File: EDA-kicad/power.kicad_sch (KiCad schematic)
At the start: 109 parts, among them Q10 NMOS, Q3 NMOS, Q3_BAT1 NMOS, Q4 NMOS, Q4_BAT1 NMOS, Q5 NMOS, Q6 NMOS, Q7 NMOS, Q8 NMOS, Q9 NMOS, SW6 CHP-041B, U10 BAT-CONNECTOR-FLTS22WR00, U11 BQ25792RQMR, U2 TPS650250RHBR

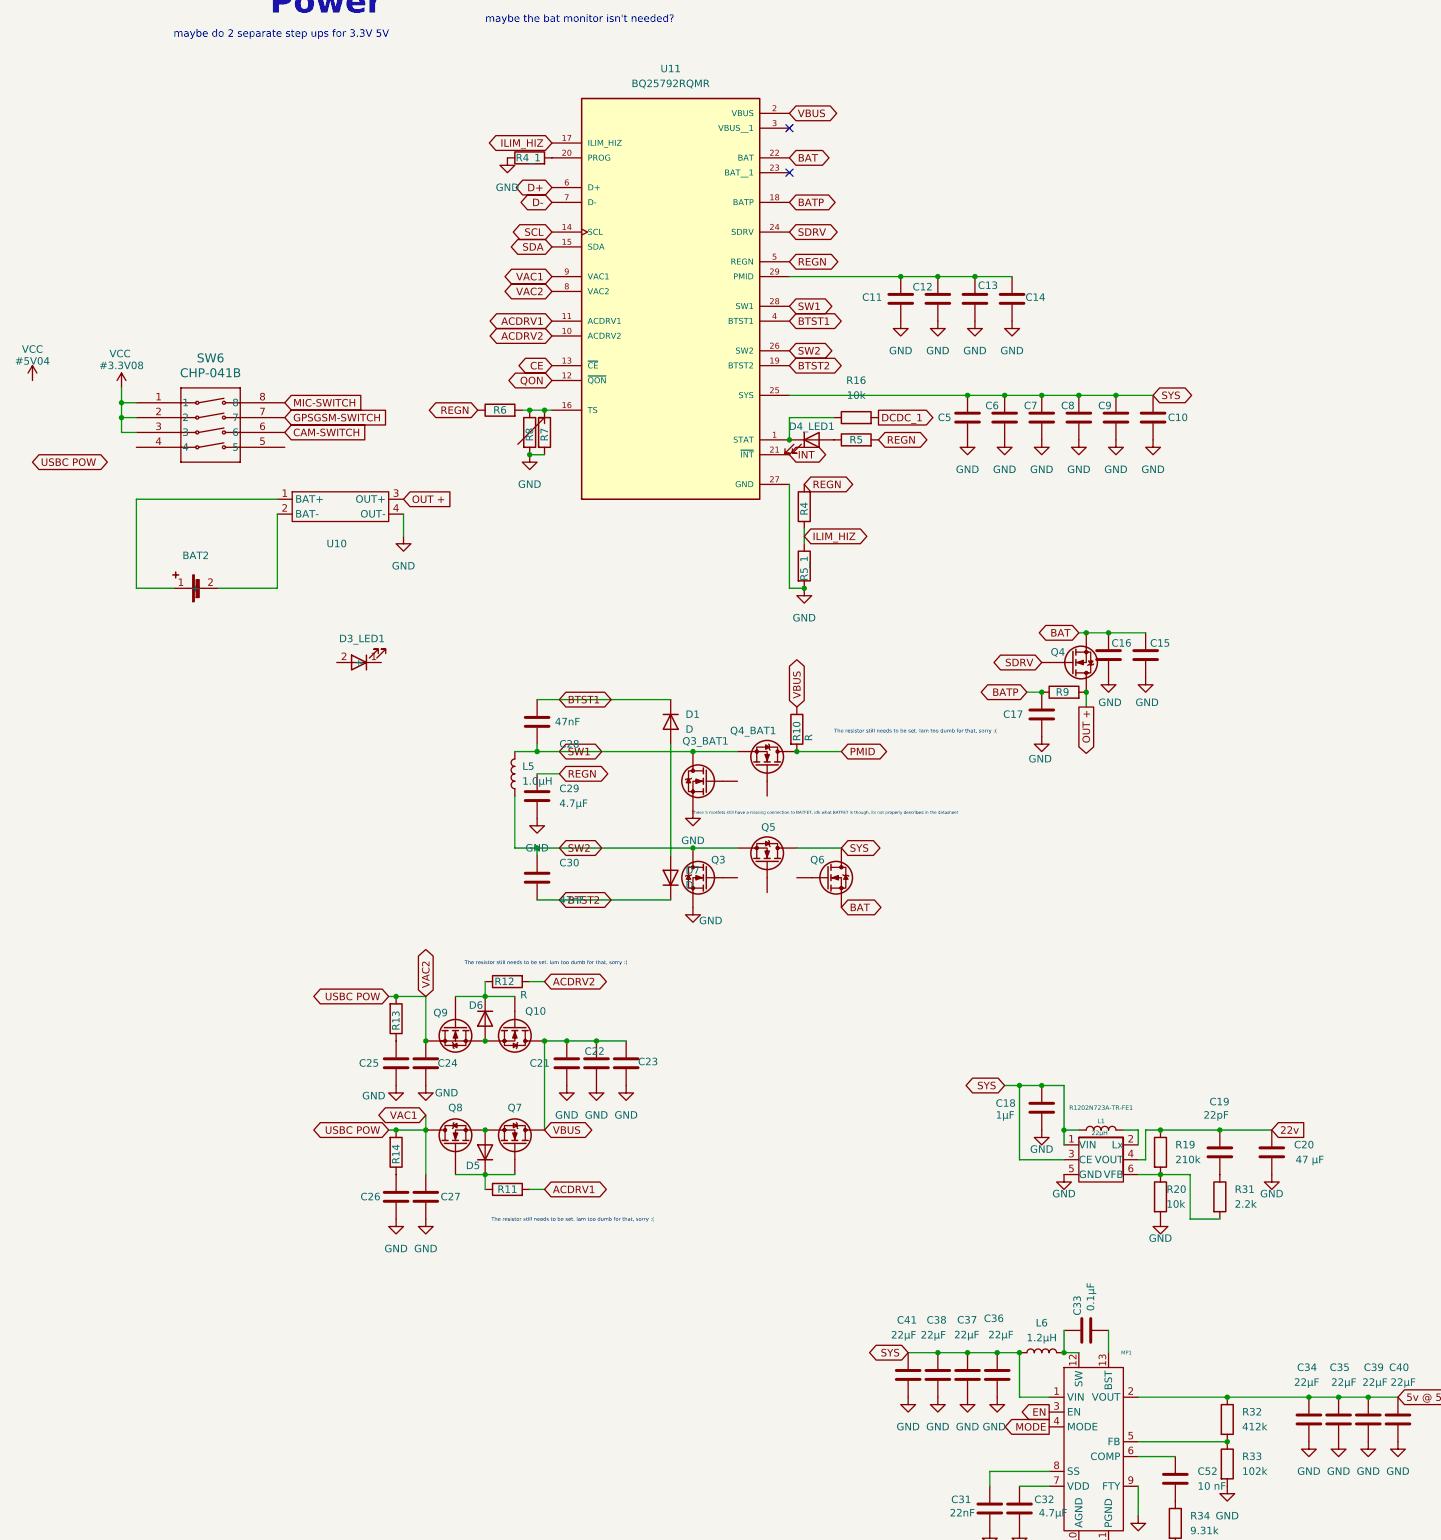
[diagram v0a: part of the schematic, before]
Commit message: fix STAT pin LED, connect USB POW, remove d3
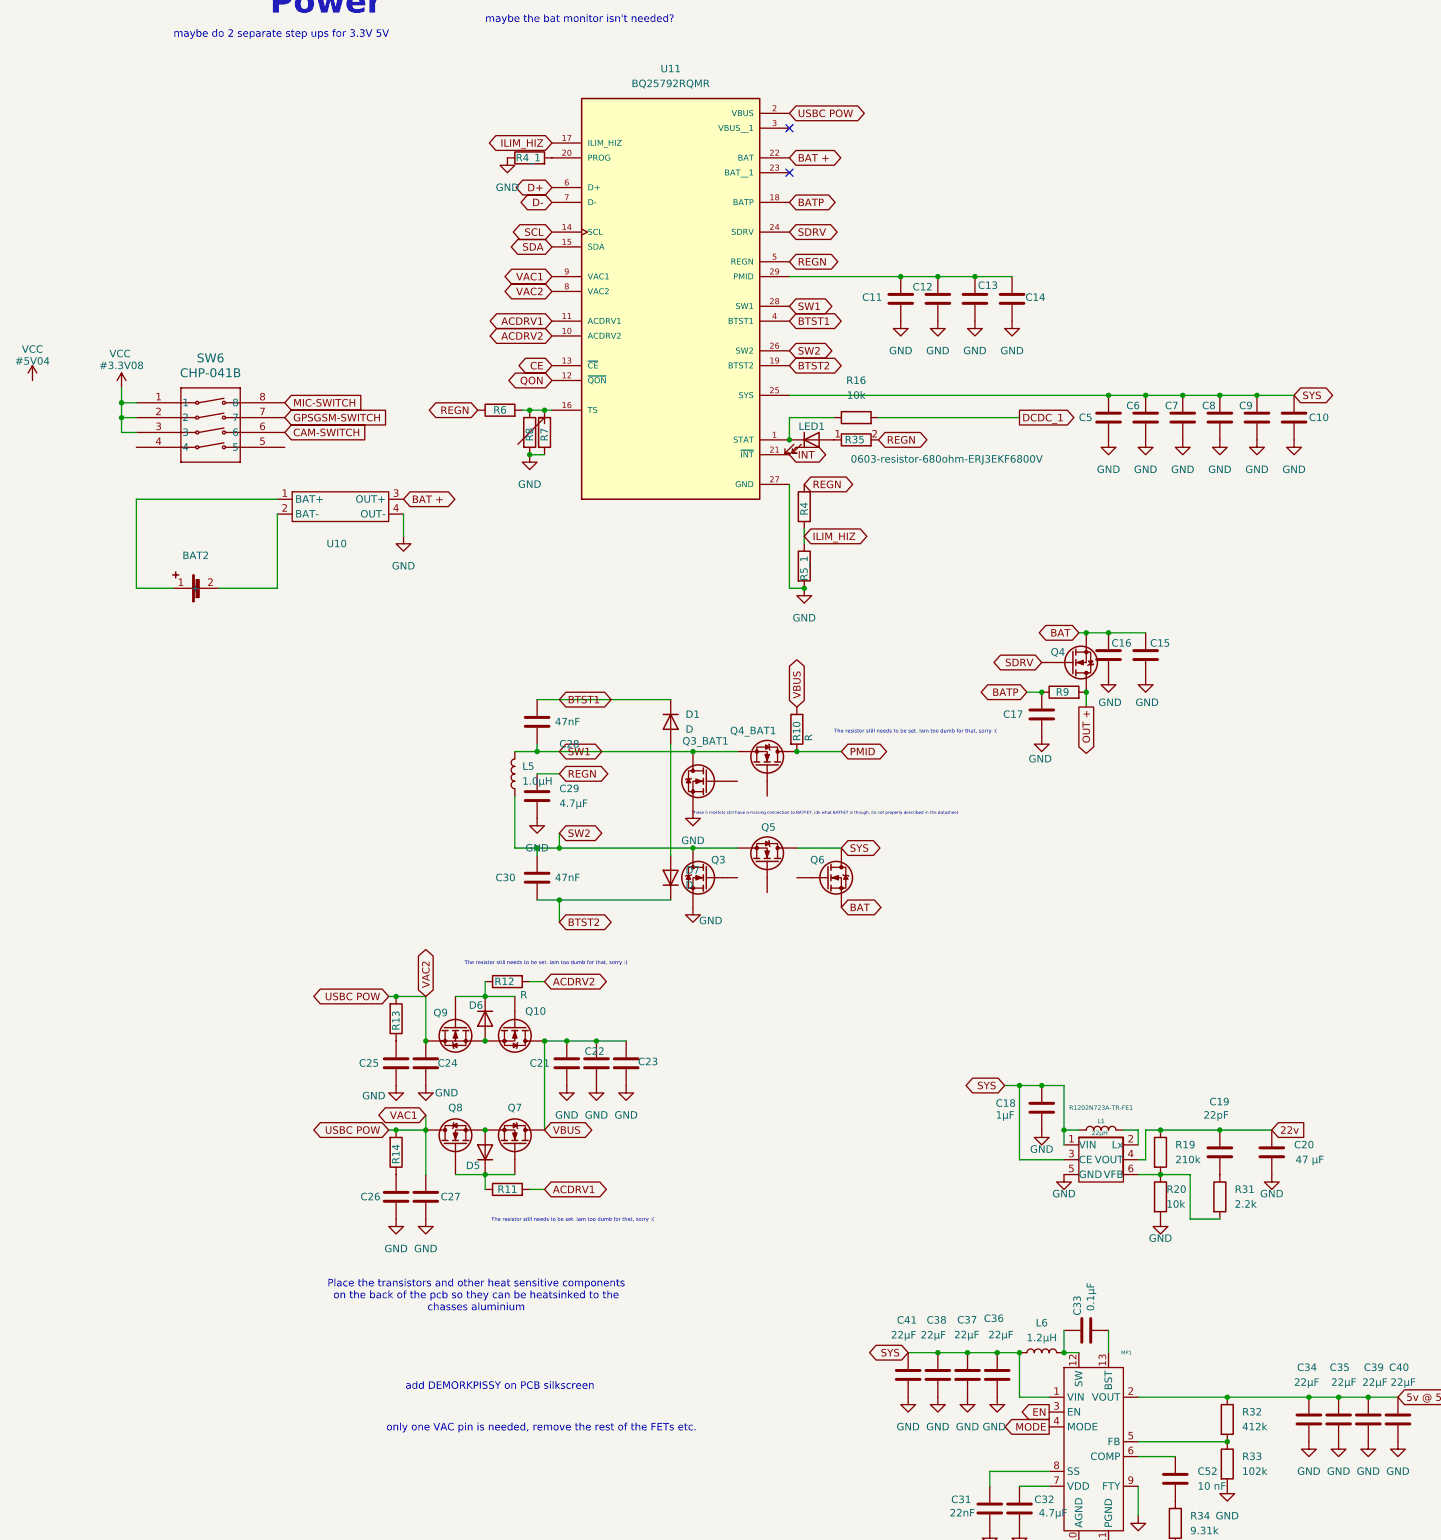
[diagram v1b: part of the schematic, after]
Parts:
- removed D3_LED1: LED-INDICATOR, SPIRIT-footprints:LED-INDICATOR, symbol SPIRIT-components:LED-INDICATOR
- removed R5: 2.2k, SPIRIT-footprints:1K-05W-0805-RES_ERJP06J102V, symbol Device:R
- added R35: 0603-resistor-680ohm-ERJ3EKF6800V, ERJ3EKF6800V:RES_ERJ3EKF6800V, symbol SPIRIT-components:0603-resistor-680ohm-ERJ3EKF6800V
- renumbered D4_LED1 to LED1
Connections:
- net BAT: no longer U11.22 (BAT)
- net OUT +: no longer U10.3 (OUT+)
- net REGN: now also R35.2
- net USBC POW: now also U11.2 (VBUS)
- net VBUS: no longer U11.2 (VBUS)
- net at LED1.2 (A): now also R35.1
- new net BAT +: U10.3 (OUT+), U11.22 (BAT)
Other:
- note added: "Place the transistors and other heat sensitive components on the back of the pcb so they can be heatsinked to the chasses aluminium"
- note added: "add DEMORKPISSY on PCB silkscreen"
- note added: "only one VAC pin is needed, remove the rest of the FETs etc."
- moved on the sheet: C10, C5, C6, C7, C8, C9

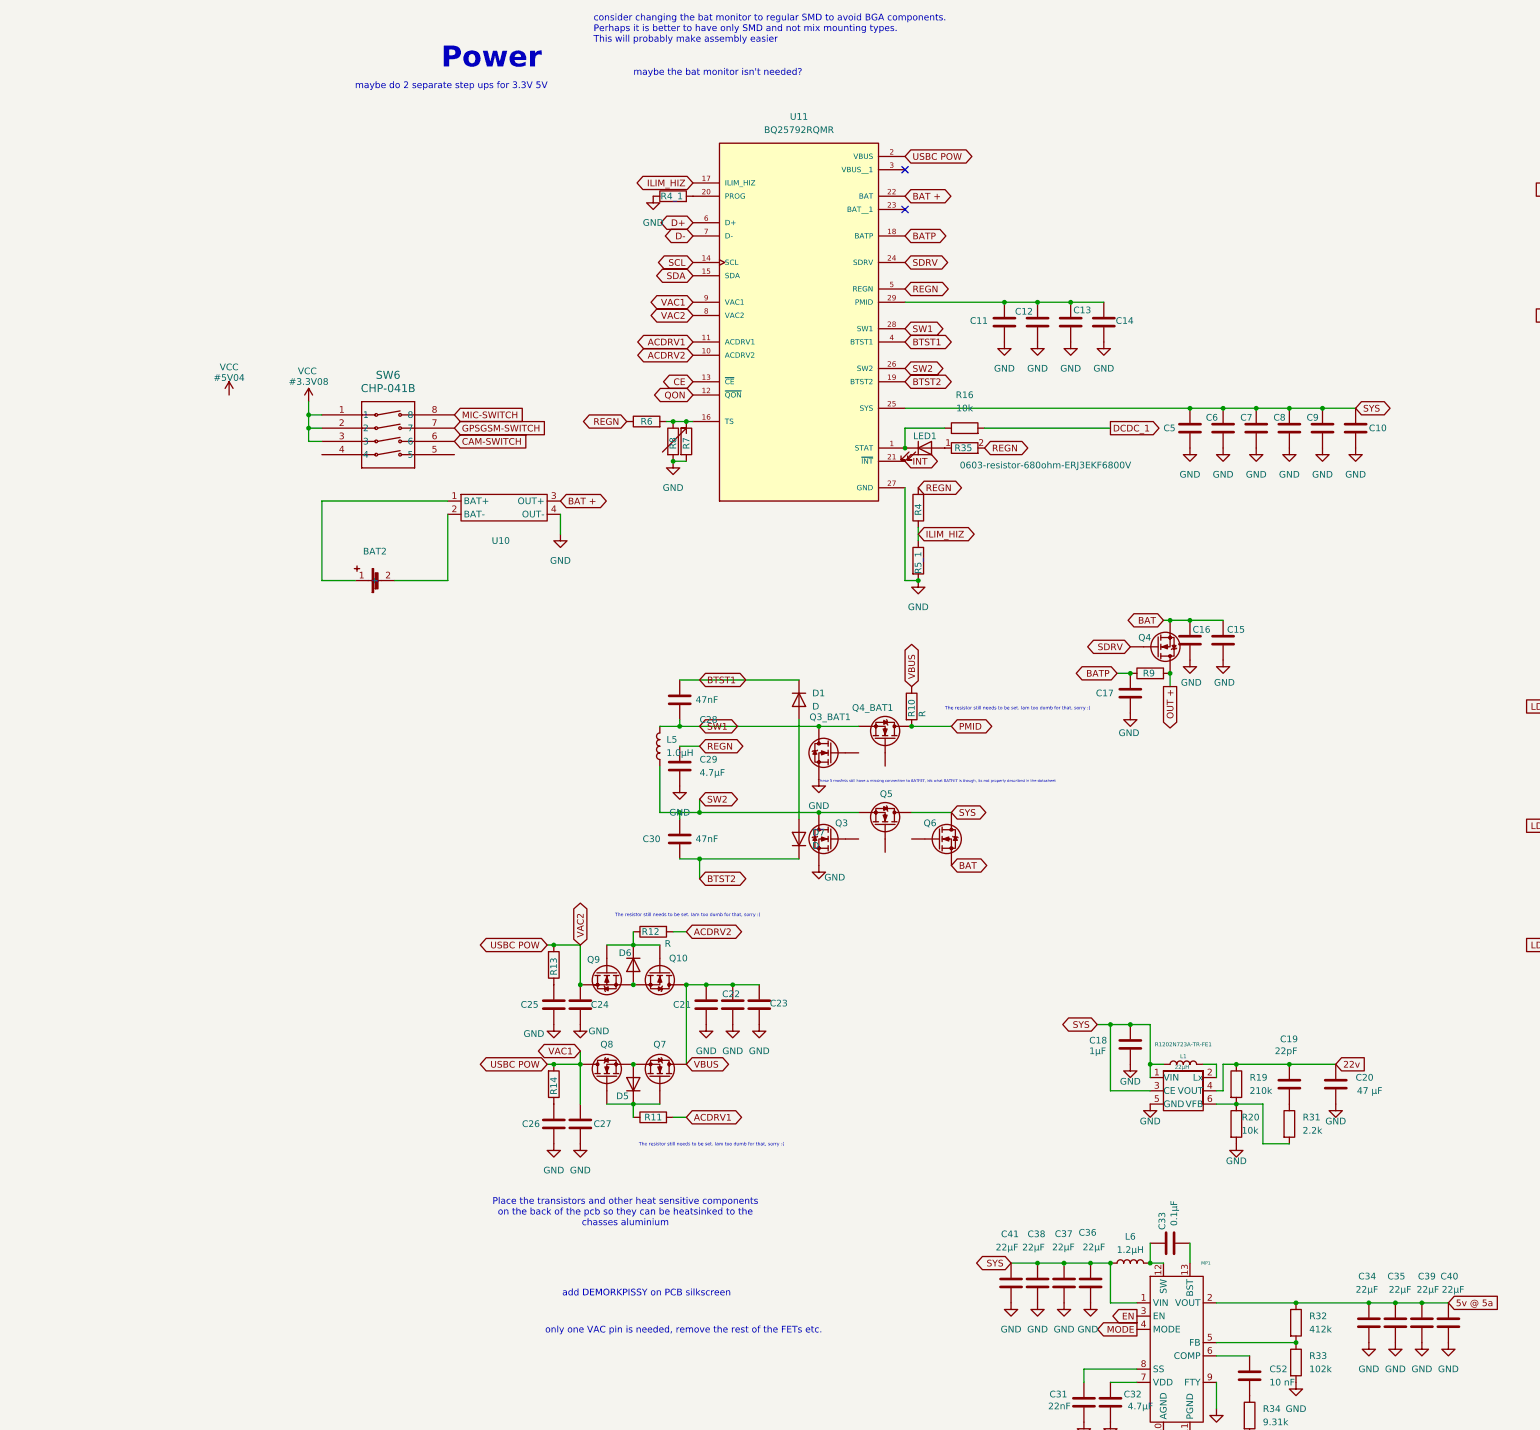
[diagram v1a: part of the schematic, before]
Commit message: connect charger IC pins 1 though 15
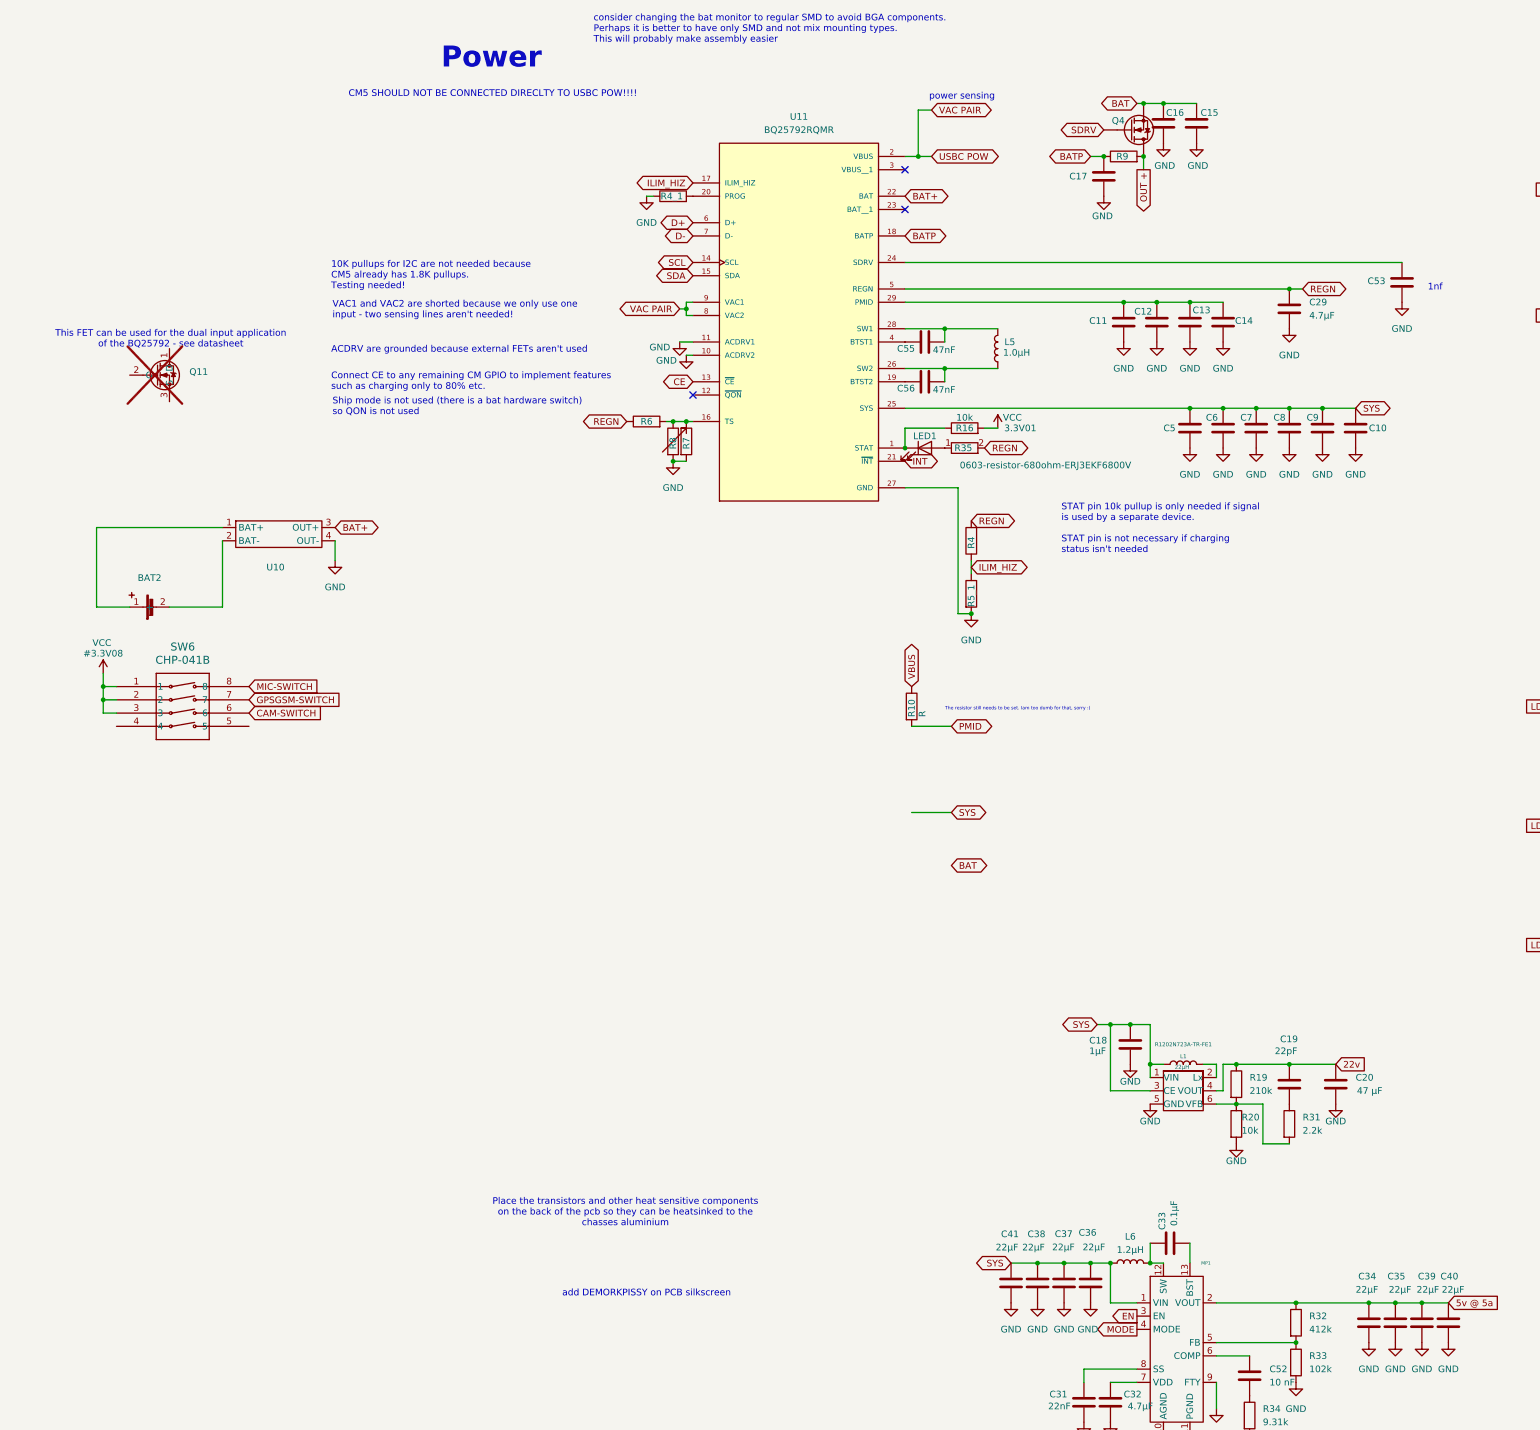
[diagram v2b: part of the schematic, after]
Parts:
- removed C21, C24, C27: 0.1μF, SPIRIT-footprints:USBC_capacitor_CAPC0603X33N, symbol Device:C
- removed C22, C23: 10μF, SPIRIT-footprints:USBC_capacitor_CAPC0603X33N, symbol Device:C
- removed C25, C26: 2.2μF, SPIRIT-footprints:USBC_capacitor_CAPC0603X33N, symbol Device:C
- removed C28, C30: 47nF, symbol Device:C
- removed D1, D7: D, symbol Device:D
- removed D5, D6: D, SPIRIT-footprints:flyback-diode-SODFL3818X130N, symbol Device:D
- removed Q10, Q3, Q3_BAT1, Q4_BAT1, Q5, Q6, Q7, Q8, Q9: NMOS, SPIRIT-footprints:gpio-driver-transistor-fix-SOT65P210X110-3N, symbol Simulation_SPICE:NMOS
- removed R11, R12: R, SPIRIT-footprints:1K-05W-0805-RES_ERJP06J102V, symbol Device:R
- removed R13, R14: 2, SPIRIT-footprints:1K-05W-0805-RES_ERJP06J102V, symbol Device:R
- added C53: 0.1μF, SPIRIT-footprints:USBC_capacitor_CAPC0603X33N, symbol Device:C
- added C55, C56: 47nF, symbol Device:C
- added Q11: ~, SPIRIT-footprints:NMOS-BSC0902NSIATMA1-PG-TDSON-8-6-IC_ISC037N03L5ISATMA1, symbol SPIRIT-components:NMOS-BSC0902NSI
- U11: EVM datasheet (none) -> https://www.ti.com/lit/ug/sluucb5e/sluucb5e.pdf?ts=17567947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
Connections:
- net ACDRV1 is gone; now on net GND: U11.11 (ACDRV1)
- net ACDRV2 is gone; now on net GND: U11.10 (ACDRV2)
- net DCDC_1 is gone; now on net VCC: R16.2
- net GND: now also C53.2
- net SDRV: no longer U11.24 (SDRV)
- net BAT + renamed BAT+
- net BTST1: no longer names the net of U11.4 (BTST1)
- net BTST1: now also C55.2
- net BTST2: no longer names the net of U11.19 (BTST2)
- net BTST2: now also C56.2
- net QON: no longer names the net of U11.12 (~{QON})
- net SW1: no longer names the net of L5.2, U11.28 (SW1)
- net SW1: now also C55.1
- net SW2: no longer names the net of L5.1, U11.26 (SW2)
- net SW2: now also C56.1
- new net: C53.1, U11.24 (SDRV)
- no-connect marks 3 -> 4
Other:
- note added: "10K pullups for I2C are not needed because CM5 already has 1.8K pullups. Testing needed!"
- note added: "1nf"
- note added: "ACDRV are grounded because external FETs aren't used"
- note added: "CM5 SHOULD NOT BE CONNECTED DIRECLTY TO USBC POW!!!!"
- note added: "Connect CE to any remaining CM GPIO to implement features such as charging only to 80% etc."
- note added: "STAT pin 10k pullup is only needed if signal is used by a separate device. STAT pin is not necessary if charging status isn't needed"
- note added: "Ship mode is not used (there is a bat hardware switch) so QON is not used"
- note added: "This FET can be used for the dual input application of the BQ25792 - see datasheet"
- note added: "VAC1 and VAC2 are shorted because we only use one input - two sensing lines aren't needed!"
- note added: "power sensing"
- note removed: "These 5 mosfets still have a missing connection to BATFET, idk what BATFET is though, its not properly described in the datasheet"
- note removed: "maybe do 2 separate step ups for 3.3V 5V"
- note removed: "maybe the bat monitor isn't needed?"
- note removed: "only one VAC pin is needed, remove the rest of the FETs etc."
- moved on the sheet: BAT2, C11, C12, C13, C14, C15, C16, C17, C29, L5, Q4, R4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
